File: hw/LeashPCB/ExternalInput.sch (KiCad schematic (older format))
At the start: 2 parts, among them J301 Conn_01x02_Male

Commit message: Changed around configuration of some parts and added top level cost estimates to block diagram
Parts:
- added SW?: SW_SPDT, symbol Switch:SW_SPDT
- J301: Link1 (none) -> https://lcsc.com/product-detail/Wire-To-Board-Wire-To-Wire-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; Standard Price 0.10 -> 0.03
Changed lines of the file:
@@
 EESchema Schematic File Version 4
-LIBS:LeashPCB-cache
 EELAYER 29 0
 EELAYER END
@@
 F 2 "Connector_JST:JST_PH_S2B-PH-SM4-TB_1x02-1MP_P2.00mm_Horizontal" H 4450 3000 50  0001 C CNN
 F 3 "~" H 4450 3000 50  0001 C CNN
-F 4 "0.10" H 4450 3000 50  0001 C CNN "Standard Price"
+F 4 "0.03" H 4450 3000 50  0001 C CNN "Standard Price"
+F 5 "https://lcsc.com/product-detail/Wire-To-Board-Wire-To-Wire-Connector_Boom-Precision-Elec-PH2-0-2PWB-2P-pitch2-0mm-Horizontal_C47647.html" H 4450 3000 50  0001 C CNN "Link1"
 	1    4450 3000
 	1    0    0    -1
@@
 Text Label 5150 3000 0    50   ~ 0
 ALT_IN
+$Comp
+L Switch:SW_SPDT SW?
+U 1 1 5D154247
+P 2900 2925
+F 0 "SW?" H 2900 3210 50  0000 C CNN
+F 1 "SW_SPDT" H 2900 3119 50  0000 C CNN
+F 2 "" H 2900 2925 50  0001 C CNN
+F 3 "~" H 2900 2925 50  0001 C CNN
+F 4 "0.05" H 2900 2925 50  0001 C CNN "Standard Price"
+	1    2900 2925
+	1    0    0    -1
+$EndComp
 $EndSCHEMATC

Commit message: Swapped out second boost for a buck. Will now take all inputs up to 5V and then buck down to 3v3 for processor
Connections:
- wire segments 4 -> 7
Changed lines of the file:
@@
 EESchema Schematic File Version 4
+LIBS:LeashPCB-cache
 EELAYER 29 0
 EELAYER END
 $Descr A4 11693 8268
 encoding utf-8
-Sheet 3 9
+Sheet 3 10
 Title ""
 Date ""
@@
 	4950 3100 4950 3450
 Wire Wire Line
-	4650 3000 5550 3000
-$Comp
-L Diode:BAT54W D301
-U 1 1 5D0807BE
-P 5700 3000
-F 0 "D301" H 5700 2775 50  0000 C CNN
-F 1 "BAT54" H 5700 2866 50  0000 C CNN
-F 2 "" H 5700 2825 50  0001 C CNN
-F 3 "" H 5700 3000 50  0001 C CNN
-	1    5700 3000
-	-1   0    0    1
-$EndComp
+	4650 3000 4950 3000
 Wire Wire Line
 	5850 3000 6550 3000
@@
 	1    0    0    -1
 $EndComp
+$Comp
+L Diode:BAT54W D301
+U 1 1 5D0807BE
+P 5700 3000
+F 0 "D301" H 5700 2775 50  0000 C CNN
+F 1 "BAT54" H 5700 2866 50  0000 C CNN
+F 2 "" H 5700 2825 50  0001 C CNN
+F 3 "" H 5700 3000 50  0001 C CNN
+	1    5700 3000
+	-1   0    0    1
+$EndComp
+Text GLabel 5100 2625 2    50   Input ~ 0
+ALT_IN
+Wire Wire Line
+	5100 2625 4950 2625
+Wire Wire Line
+	4950 2625 4950 3000
+Connection ~ 4950 3000
+Wire Wire Line
+	4950 3000 5550 3000
 $EndSCHEMATC

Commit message: Added more top level signals to block diagram and added alternate population options for power
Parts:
- removed SW?: SW_SPDT, symbol Switch:SW_SPDT
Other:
- note added: "No pop if using the \nswitch/jumper method"
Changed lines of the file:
@@
 ALT_IN
-$Comp
-L Switch:SW_SPDT SW?
-U 1 1 5D154247
-P 2900 2925
-F 0 "SW?" H 2900 3210 50  0000 C CNN
-F 1 "SW_SPDT" H 2900 3119 50  0000 C CNN
-F 2 "" H 2900 2925 50  0001 C CNN
-F 3 "~" H 2900 2925 50  0001 C CNN
-F 4 "0.05" H 2900 2925 50  0001 C CNN "Standard Price"
-	1    2900 2925
-	1    0    0    -1
-$EndComp
 $Comp
 L Diode:BAT54W D301
@@
 Wire Wire Line
 	4950 3000 5550 3000
+Text Notes 5375 3300 0    50   ~ 0
+No pop if using the \nswitch/jumper method
 $EndSCHEMATC

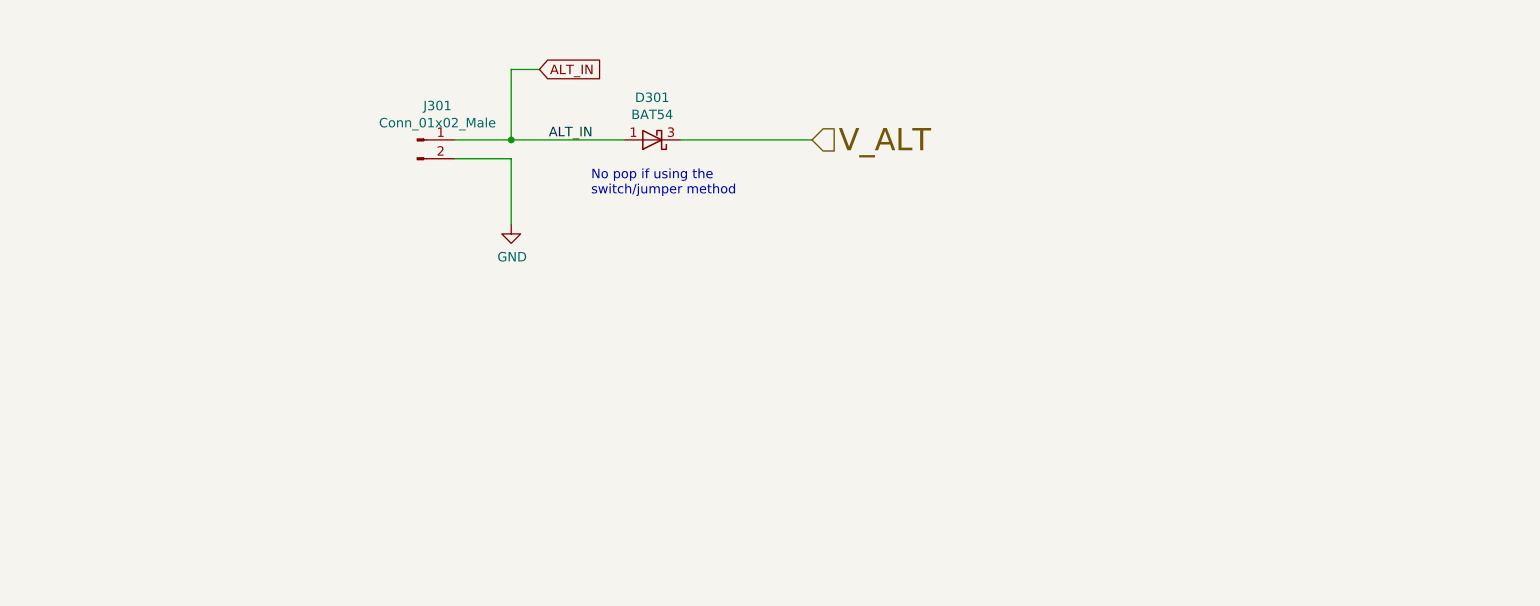
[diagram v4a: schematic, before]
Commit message: Resized schematic sheets for printing and remapped signals for matching Launchpad headers
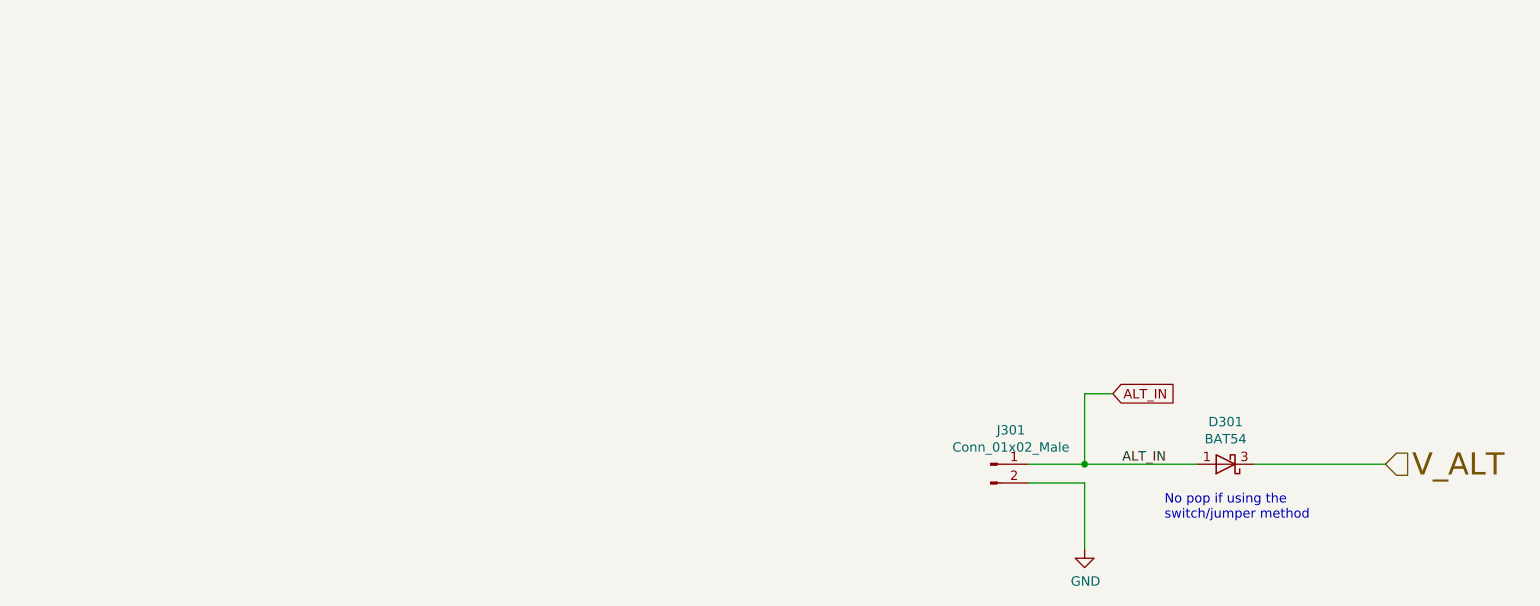
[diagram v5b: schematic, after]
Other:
- moved on the sheet: D301, J301
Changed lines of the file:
@@
 EESchema Schematic File Version 4
+LIBS:LeashPCB-cache
 EELAYER 29 0
 EELAYER END
-$Descr A4 11693 8268
+$Descr B 17000 11000
 encoding utf-8
 Sheet 3 10
-Title ""
-Date ""
-Rev ""
-Comp ""
-Comment1 ""
+Title "BeagleDust Leash PCB"
+Date "2019-07-22"
+Rev "1"
+Comp "Beagleboard.org"
+Comment1 "Schematic designed by Analog Life, LLC"
 Comment2 ""
 Comment3 ""
@@
 L Connector:Conn_01x02_Male J?
 U 1 1 5D080251
-P 4450 3000
+P 7500 4725
 AR Path="/5D080251" Ref="J?"  Part="1"
 AR Path="/5D0603E8/5D080251" Ref="J301"  Part="1"
-F 0 "J301" H 4558 3181 50  0000 C CNN
-F 1 "Conn_01x02_Male" H 4558 3090 50  0000 C CNN
-F 2 "Connector_JST:JST_PH_S2B-PH-SM4-TB_1x02-1MP_P2.00mm_Horizontal" H 4450 3000 50  0001 C CNN
-F 3 "~" H 4450 3000 50  0001 C CNN
-F 4 "0.03" H 4450 3000 50  0001 C CNN "Standard Price"
-F 5 "https://lcsc.com/product-detail/Wire-To-Board-Wire-To-Wire-Connector_Boom-Precision-Elec-PH2-0-2PWB-2P-pitch2-0mm-Horizontal_C47647.html" H 4450 3000 50  0001 C CNN "Link1"
-	1    4450 3000
+F 0 "J301" H 7608 4906 50  0000 C CNN
+F 1 "Conn_01x02_Male" H 7608 4815 50  0000 C CNN
+F 2 "Connector_JST:JST_PH_S2B-PH-SM4-TB_1x02-1MP_P2.00mm_Horizontal" H 7500 4725 50  0001 C CNN
+F 3 "~" H 7500 4725 50  0001 C CNN
+F 4 "0.03" H 7500 4725 50  0001 C CNN "Standard Price"
+F 5 "https://lcsc.com/product-detail/Wire-To-Board-Wire-To-Wire-Connector_Boom-Precision-Elec-PH2-0-2PWB-2P-pitch2-0mm-Horizontal_C47647.html" H 7500 4725 50  0001 C CNN "Link1"
+	1    7500 4725
 	1    0    0    -1
 $EndComp
 Wire Wire Line
-	4650 3100 4950 3100
+	7700 4825 8000 4825
 $Comp
 L power:GND #PWR?
 U 1 1 5D080259
-P 4950 3450
+P 8000 5175
 AR Path="/5D080259" Ref="#PWR?"  Part="1"
 AR Path="/5D0603E8/5D080259" Ref="#PWR0301"  Part="1"
-F 0 "#PWR0301" H 4950 3200 50  0001 C CNN
-F 1 "GND" H 4955 3277 50  0000 C CNN
-F 2 "" H 4950 3450 50  0001 C CNN
-F 3 "" H 4950 3450 50  0001 C CNN
-	1    4950 3450
+F 0 "#PWR0301" H 8000 4925 50  0001 C CNN
+F 1 "GND" H 8005 5002 50  0000 C CNN
+F 2 "" H 8000 5175 50  0001 C CNN
+F 3 "" H 8000 5175 50  0001 C CNN
+	1    8000 5175
 	1    0    0    -1
 $EndComp
 Wire Wire Line
-	4950 3100 4950 3450
+	8000 4825 8000 5175
 Wire Wire Line
-	4650 3000 4950 3000
+	7700 4725 8000 4725
 Wire Wire Line
-	5850 3000 6550 3000
-Text HLabel 6550 3000 2    118  Input ~ 0
+	8900 4725 9600 4725
+Text HLabel 9600 4725 2    118  Input ~ 0
 V_ALT
-Text Label 5150 3000 0    50   ~ 0
+Text Label 8200 4725 0    50   ~ 0
 ALT_IN
 $Comp
 L Diode:BAT54W D301
 U 1 1 5D0807BE
-P 5700 3000
-F 0 "D301" H 5700 2775 50  0000 C CNN
-F 1 "BAT54" H 5700 2866 50  0000 C CNN
-F 2 "" H 5700 2825 50  0001 C CNN
-F 3 "" H 5700 3000 50  0001 C CNN
-	1    5700 3000
+P 8750 4725
+F 0 "D301" H 8750 4500 50  0000 C CNN
+F 1 "BAT54" H 8750 4591 50  0000 C CNN
+F 2 "" H 8750 4550 50  0001 C CNN
+F 3 "" H 8750 4725 50  0001 C CNN
+	1    8750 4725
 	-1   0    0    1
 $EndComp
-Text GLabel 5100 2625 2    50   Input ~ 0
+Text GLabel 8150 4350 2    50   Input ~ 0
 ALT_IN
 Wire Wire Line
-	5100 2625 4950 2625
+	8150 4350 8000 4350
 Wire Wire Line
-	4950 2625 4950 3000
-Connection ~ 4950 3000
+	8000 4350 8000 4725
+Connection ~ 8000 4725
 Wire Wire Line
-	4950 3000 5550 3000
-Text Notes 5375 3300 0    50   ~ 0
+	8000 4725 8600 4725
+Text Notes 8425 5025 0    50   ~ 0
 No pop if using the \nswitch/jumper method
 $EndSCHEMATC

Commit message: Pulled in final small components and finished routing all but the RF section
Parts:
- D301: footprint (none) -> Diode_SMD:D_SOD-123; symbol Diode:BAT54W -> Device:D_Schottky
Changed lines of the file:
@@
 ALT_IN
 $Comp
-L Diode:BAT54W D301
+L Device:D_Schottky D301
 U 1 1 5D0807BE
 P 8750 4725
 F 0 "D301" H 8750 4500 50  0000 C CNN
 F 1 "BAT54" H 8750 4591 50  0000 C CNN
-F 2 "" H 8750 4550 50  0001 C CNN
+F 2 "Diode_SMD:D_SOD-123" H 8750 4550 50  0001 C CNN
 F 3 "" H 8750 4725 50  0001 C CNN
 	1    8750 4725

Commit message: Hooked up RX/TX to the USB converter (whoops) and added a few other small connections.
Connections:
- wire segments 7 -> 4
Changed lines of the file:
@@
 	8000 4825 8000 5175
-Wire Wire Line
-	7700 4725 8000 4725
 Wire Wire Line
 	8900 4725 9600 4725
@@
 	-1   0    0    1
 $EndComp
-Text GLabel 8150 4350 2    50   Input ~ 0
-ALT_IN
-Wire Wire Line
-	8150 4350 8000 4350
-Wire Wire Line
-	8000 4350 8000 4725
-Connection ~ 8000 4725
-Wire Wire Line
-	8000 4725 8600 4725
 Text Notes 8425 5025 0    50   ~ 0
 No pop if using the \nswitch/jumper method
+Wire Wire Line
+	7700 4725 8600 4725
 $EndSCHEMATC
